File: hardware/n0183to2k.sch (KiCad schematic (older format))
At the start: 40 parts, among them J1 NMEA0183 (wind), J2 Conn_01x06_Male, J3 Conn_01x05_Male, J4 RJ45, J5 RJ45, J6 Conn_02x03_Odd_Even, Q1 BSS123, Q2 DMG2307L, Q3 BSS123, U1 PIC18F27Q84_ISS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

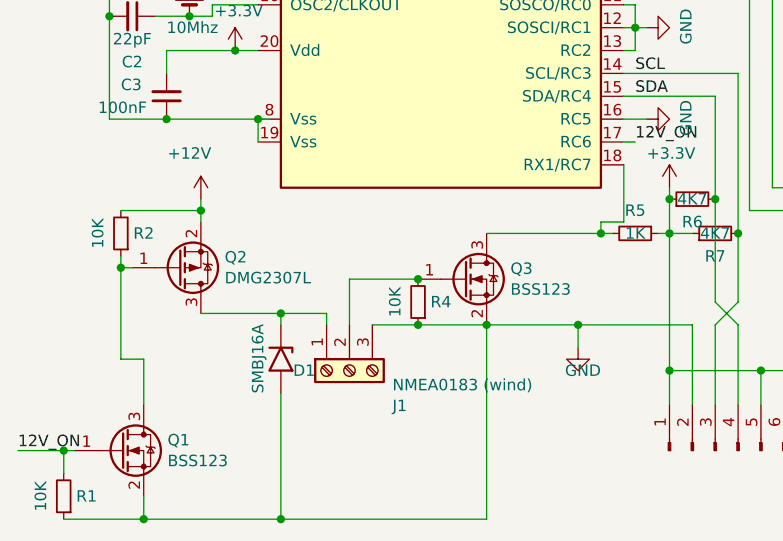
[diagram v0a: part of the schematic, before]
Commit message: Add a smbj16a on the nmea0183 data line too.
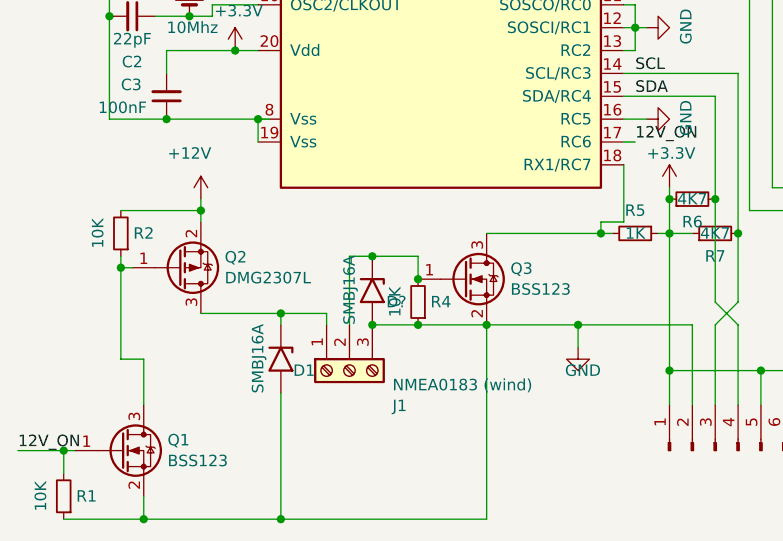
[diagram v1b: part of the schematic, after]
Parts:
- added D?: SMBJ16A, Diode_SMD:D_SMB_Handsoldering, symbol Diode:1.5KExxA
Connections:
- net GND: now also D?.2 (A2)
- net at J1.2 (Pin_2), Q3.1 (G), R4.2: now also D?.1 (A1)
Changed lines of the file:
@@
 $EndComp
 Connection ~ 2950 6050
-Wire Wire Line
-	2650 5850 2350 5850
-Wire Wire Line
-	2350 5850 2350 6050
 $Comp
 L power:+12V #PWR03
@@
 	1    0    0    -1
 $EndComp
-Connection ~ 2650 5850
 Wire Wire Line
 	2650 6050 2950 6050
@@
 	1    0    0    -1
 $EndComp
+$Comp
+L Diode:1.5KExxA D?
+U 1 1 622C1983
+P 2450 5900
+F 0 "D?" V 2500 6050 50  0000 R CNN
+F 1 "SMBJ16A" H 2600 5800 50  0000 R CNN
+F 2 "Diode_SMD:D_SMB_Handsoldering" H 2450 5700 50  0001 C CNN
+F 3 "https://www.vishay.com/docs/88301/15ke.pdf" H 2400 5900 50  0001 C CNN
+	1    2450 5900
+	0    1    1    0
+$EndComp
+Connection ~ 2450 6050
+Wire Wire Line
+	2450 5750 2350 5750
+Wire Wire Line
+	2350 5750 2350 6050
+Wire Wire Line
+	2450 5750 2650 5750
+Wire Wire Line
+	2650 5750 2650 5850
+Connection ~ 2450 5750
+Connection ~ 2650 5850
 $EndSCHEMATC

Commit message: Annotate
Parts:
- gave numbers to parts that had none: 1
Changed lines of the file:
@@
 $EndComp
 $Comp
-L Diode:1.5KExxA D?
+L Diode:1.5KExxA D4
 U 1 1 622C1983
 P 2450 5900
-F 0 "D?" V 2500 6050 50  0000 R CNN
+F 0 "D4" V 2500 6050 50  0000 R CNN
 F 1 "SMBJ16A" H 2600 5800 50  0000 R CNN
 F 2 "Diode_SMD:D_SMB_Handsoldering" H 2450 5700 50  0001 C CNN

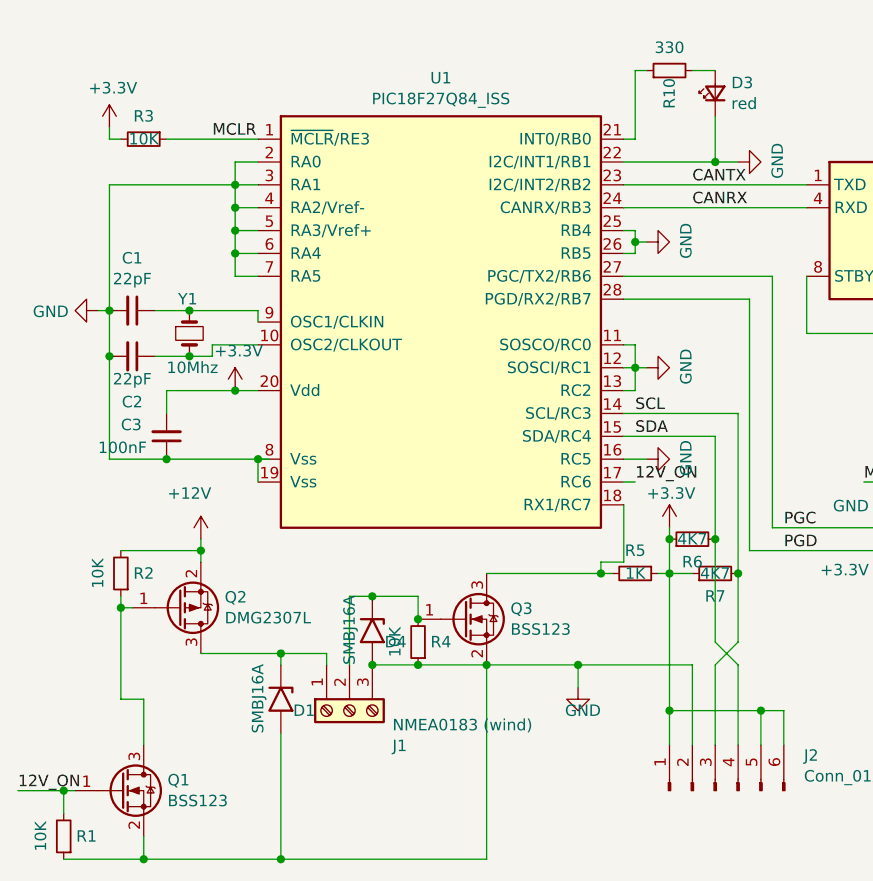
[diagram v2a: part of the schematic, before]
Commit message: move 12V_ON to RA2, closer to the mosfet.
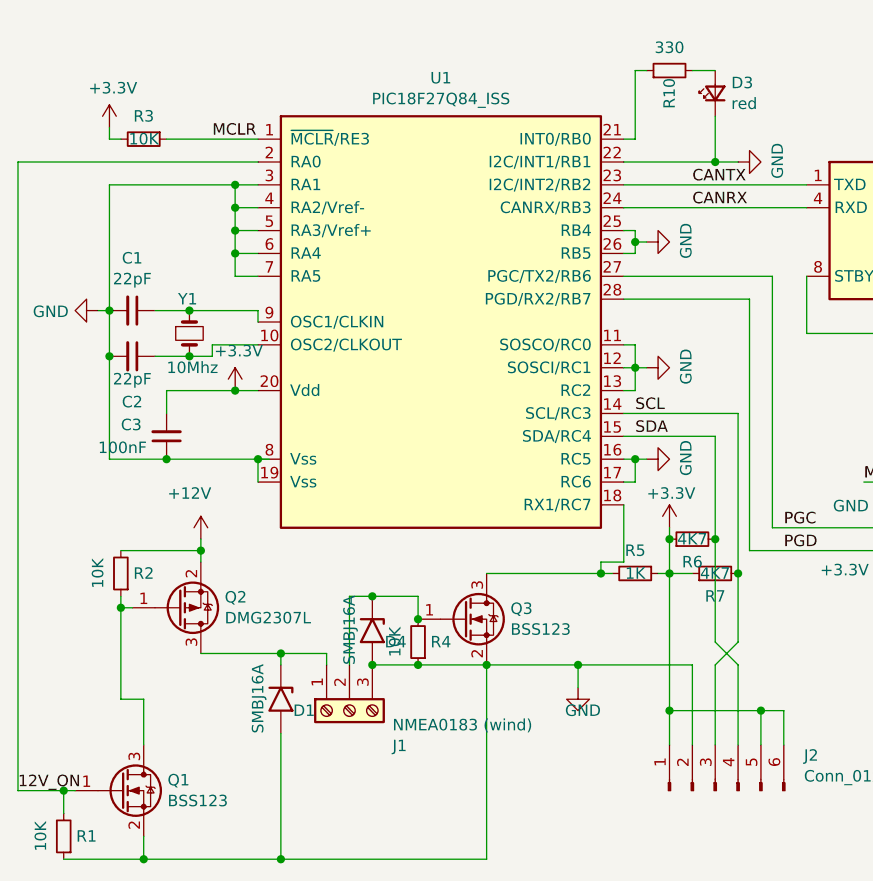
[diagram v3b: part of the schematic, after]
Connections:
- net 12V_ON: now also U1.2 (RA0); no longer U1.17 (RC6)
- net GND: now also U1.17 (RC6); no longer U1.2 (RA0)
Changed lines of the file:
@@
 $EndComp
 Wire Wire Line
-	3650 5150 3550 5150
+	3650 5150 3600 5150
 Text Label 3600 4950 0    50   ~ 0
 SCL
@@
 	900  6600 1100 6600
 Connection ~ 1100 6600
-Text Label 3600 5250 0    50   ~ 0
-12V_ON
 Wire Wire Line
 	3600 5250 3550 5250
@@
 	3600 4200 3600 4250
 Wire Wire Line
-	1950 3850 1850 3850
-Wire Wire Line
-	1850 3850 1850 3950
-Wire Wire Line
 	1850 4350 1950 4350
 Wire Wire Line
@@
 Connection ~ 2450 5750
 Connection ~ 2650 5850
+Wire Wire Line
+	1950 3850 900  3850
+Wire Wire Line
+	900  3850 900  6600
+Wire Wire Line
+	3600 5250 3600 5150
+Connection ~ 3600 5150
+Wire Wire Line
+	3600 5150 3550 5150
 $EndSCHEMATC

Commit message: replace a SMD resistor with a though-hole to avoid a jumper, and finish routing
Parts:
- R7: footprint Resistor_SMD:R_0805_2012Metric_Pad1.20x1.40mm_HandSolder -> Resistor_THT:R_Axial_DIN0207_L6.3mm_D2.5mm_P7.62mm_Horizontal
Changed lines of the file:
@@
 F 0 "R7" V 3850 5650 50  0000 C CNN
 F 1 "4K7" V 3950 5650 50  0000 C CNN
-F 2 "Resistor_SMD:R_0805_2012Metric_Pad1.20x1.40mm_HandSolder" H 3950 5650 50  0001 C CNN
+F 2 "Resistor_THT:R_Axial_DIN0207_L6.3mm_D2.5mm_P7.62mm_Horizontal" H 3950 5650 50  0001 C CNN
 F 3 "~" H 3950 5650 50  0001 C CNN
 	1    3950 5650
